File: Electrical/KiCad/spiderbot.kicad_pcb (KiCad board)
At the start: 2 copper layers, 70 x 80 mm, 136 parts, among them J1 Ras Pi 4 Interface, J10 Conn_01x03, J11 Conn_01x03, J12 Conn_01x03, J13 Conn_01x03, J14 Conn_01x03, J15 Conn_01x03, J16 Conn_01x03, J17 Conn_01x03, J18 Conn_01x03, J19 Conn_01x03, J2 Leg Switches, J20 Conn_01x03, J21 Conn_01x03, J22 Conn_01x03, J23 Conn_01x03, J24 Conn_01x03, J25 Conn_01x03, J26 Conn_01x03, J27 Conn_01x03, J28 5V to 6V Connect, J3 5V Connect, J4 Terminal Block, J5 6V Connect, J6 Conn_01x03, J7 Conn_01x03, J8 Conn_01x03, J9 Conn_01x03, Q1 CSD17304Q3, Q2 CSD17304Q3, Q3 CSD13202Q2, Q4 BSS138, Q5 BSS138, Q6 BSS138, U1 TLVM13640RDLR, U2 TPS40305DRCR, U3 LM393, U4 PCA9685PW, U5 PCA9685PW, U6 LSM6DSO32TR

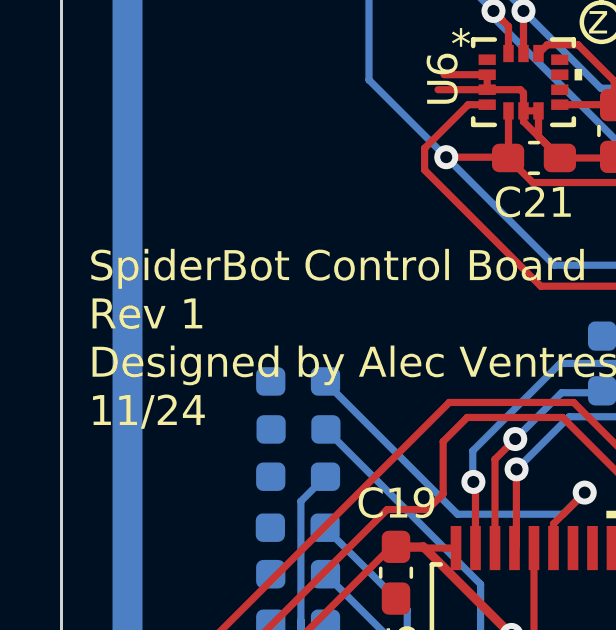
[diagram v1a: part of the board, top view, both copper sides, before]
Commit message: Finished Rev2 of the PCB
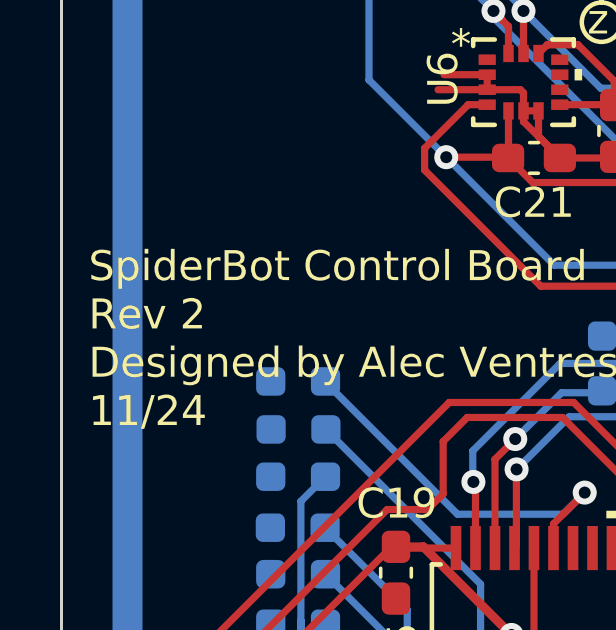
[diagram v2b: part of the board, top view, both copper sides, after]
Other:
- board text added: "SpiderBot Control Board Rev 2 Designed by Alec Ventresca :) 11/24"
- board text removed: "SpiderBot Control Board Rev 1 Designed by Alec Ventresca :) 11/24"
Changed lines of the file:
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@@
 		)
 	)
-	(gr_text "SpiderBot Control Board\nRev 1\nDesigned by Alec Ventresca :)\n11/24"
+	(gr_text "SpiderBot Control Board\nRev 2\nDesigned by Alec Ventresca :)\n11/24"
 		(at -5.5 36.05 0)
 		(layer "F.SilkS")
